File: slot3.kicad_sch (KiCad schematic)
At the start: 1 part

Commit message: board layout
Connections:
- net AD1: now also PL3.a3 (Pin_a3); no longer PL3.b3 (Pin_b3)
- net Chroma: now also PL3.a2 (Pin_a2); no longer PL3.b2 (Pin_b2)
- net GND: now also PL3.b3 (Pin_b3); no longer PL3.a3 (Pin_a3)
- net Luma: now also PL3.b2 (Pin_b2); no longer PL3.a2 (Pin_a2)
- net VCLK: now reaches PL3.a38 (Pin_a38)
- net ESND: now reaches PL3.b10 (Pin_b10)
- no-connect marks 1 -> 0

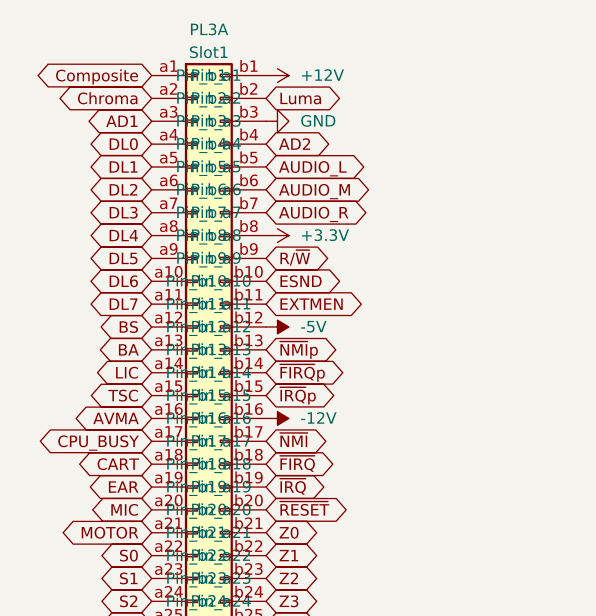
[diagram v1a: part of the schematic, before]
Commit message: revise bus tracing
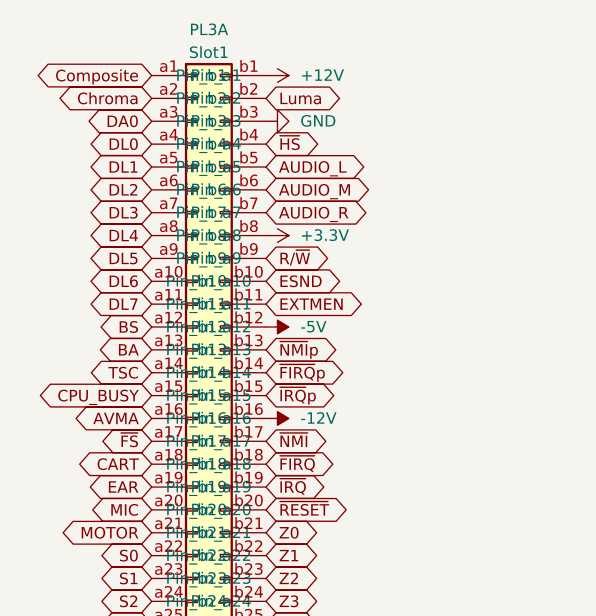
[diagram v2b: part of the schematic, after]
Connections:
- net LIC is gone; now on net TSC: PL3.a14 (Pin_a14)
- net CPU_BUSY: now also PL3.a15 (Pin_a15); no longer PL3.a17 (Pin_a17)
- net TSC: no longer PL3.a15 (Pin_a15)
- net AD1 renamed DA0
- net AD2 renamed ~{HS}
- new net ~{FS}: PL3.a17 (Pin_a17)
